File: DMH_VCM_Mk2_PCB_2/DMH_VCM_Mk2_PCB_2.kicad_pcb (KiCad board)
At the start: 2 copper layers, 48 x 175 mm, 95 parts, among them J1 TS_Jack_6.35mm_Sw, J10 TS_Jack_6.35mm_Sw, J100 IDC_02x05, J2 TS_Jack_6.35mm_Sw, J200 IDC_02x05, J3 TS_Jack_6.35mm_Sw, J4 TS_Jack_6.35mm_Sw, J5 TS_Jack_6.35mm_Sw, J50 Conn_01x08, J6 TS_Jack_6.35mm_Sw, J60 Conn_01x08, J7 TS_Jack_6.35mm_Sw, J70 Conn_01x08, J8 TS_Jack_6.35mm_Sw, J9 TS_Jack_6.35mm_Sw, Q1 BC548, Q2 BC548, Q3 BC548, Q4 BC548, Q5 BC548, Q6 BC548, U1 TL074, U2 TL074, U3 TL074

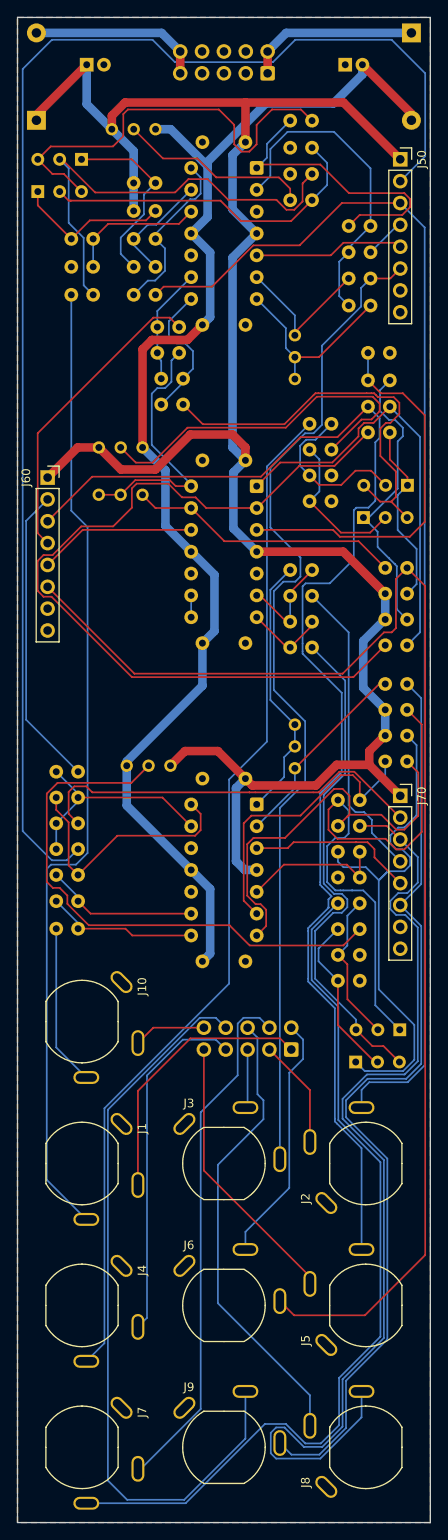
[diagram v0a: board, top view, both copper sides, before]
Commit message: Positioned PCB 2 components
Volume conflict with headers, needs correction o PCB 1
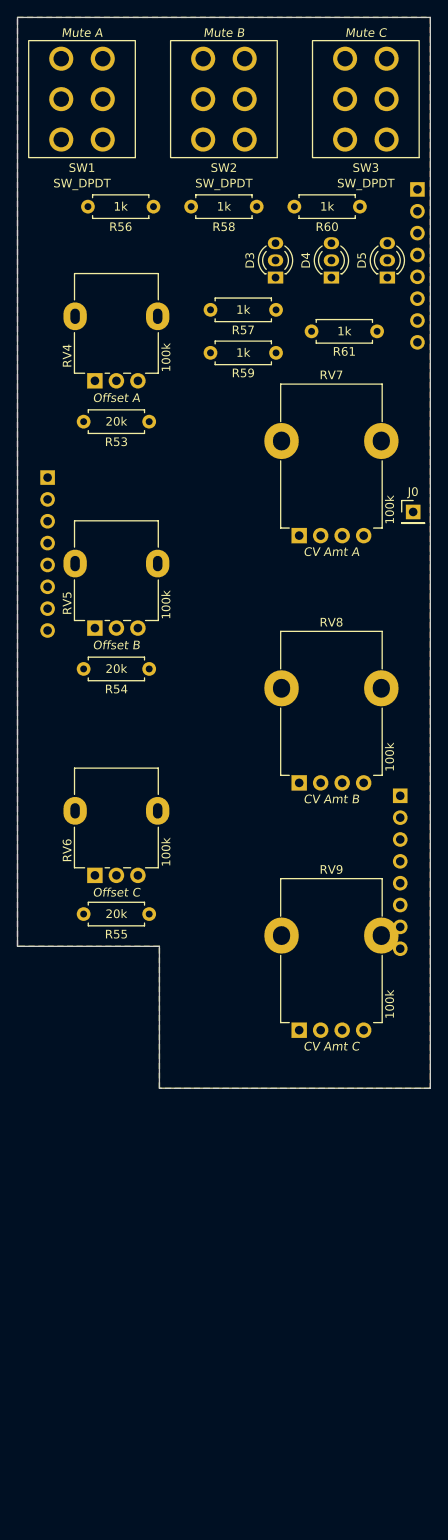
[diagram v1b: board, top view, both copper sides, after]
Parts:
- removed C1, C2: 47uF, Capacitor_THT:CP_Radial_D5.0mm_P2.00mm
- removed C3, C4, C5, C6, C7, C8: 100nF, Capacitor_THT:C_Disc_D4.3mm_W1.9mm_P5.00mm
- removed D1: SB140+, Diode_THT:D_DO-41_SOD81_P10.16mm_Horizontal
- removed D2: SB140-, Diode_THT:D_DO-41_SOD81_P10.16mm_Horizontal
- removed J1, J10, J2, J3, J4, J5, J6, J7, J8, J9: TS_Jack_6.35mm_Sw, SynthStuff:CUI_MJ-63052A
- removed J100: IDC_02x05, SynthStuff:IDC-Header_2x05_P2.54mm_Vertical_Eurorack
- removed J200: IDC_02x05, SynthStuff:IDC-Header_2x05_P2.54mm_Vertical_BackBone
- removed Q1, Q2, Q3, Q4, Q5, Q6: BC548, Package_TO_SOT_THT:TO-92L_Inline_Wide
- removed R1, R16, R17, R2, R31, R32: 20k, Resistor_THT:R_Axial_DIN0207_L6.3mm_D2.5mm_P2.54mm_Vertical
- removed R10, R11, R25, R26, R40, R41: 100R, Resistor_THT:R_Axial_DIN0207_L6.3mm_D2.5mm_P2.54mm_Vertical
- removed R12, R19, R21, R27, R34, R36, R4, R42, R6: 10k, Resistor_THT:R_Axial_DIN0207_L6.3mm_D2.5mm_P2.54mm_Vertical
- removed R13, R28, R62: 33k, Resistor_THT:R_Axial_DIN0207_L6.3mm_D2.5mm_P2.54mm_Vertical
- removed R14, R15, R18, R22, R23, R24, R29, R3, R30, R33, R37, R38, R39, R44, R45, R46, R47, R48, R49, R50, R51, R63, R64, R65, R7, R8, R9: 100k, Resistor_THT:R_Axial_DIN0207_L6.3mm_D2.5mm_P2.54mm_Vertical
- removed R20, R35, R5, R52: 1k, Resistor_THT:R_Axial_DIN0207_L6.3mm_D2.5mm_P2.54mm_Vertical
- removed RV1, RV2, RV3: 100k, Potentiometer_THT:Potentiometer_Bourns_3296W_Vertical
- removed RV10, RV11, RV12: 50k, Potentiometer_THT:Potentiometer_Bourns_3296W_Vertical
- removed U1, U2, U3: TL074, Package_DIP:DIP-14_W7.62mm_Socket
- added D3: LED_Dual_AKA, SynthStuff:LED_D3.0mm-2color, F.Cu at (81.0, 70.8)
- added D4: LED_Dual_AKA, SynthStuff:LED_D3.0mm-2color, F.Cu at (87.5, 70.8)
- added D5: LED_Dual_AKA, SynthStuff:LED_D3.0mm-2color, F.Cu at (94.0, 70.8)
- added J0: Conn_01x01, Connector_PinHeader_2.54mm:PinHeader_1x01_P2.54mm_Vertical, F.Cu at (97.0, 100.0)
- added R53: 20k, Resistor_THT:R_Axial_DIN0207_L6.3mm_D2.5mm_P7.62mm_Horizontal, F.Cu at (66.3, 89.5)
- added R54: 20k, Resistor_THT:R_Axial_DIN0207_L6.3mm_D2.5mm_P7.62mm_Horizontal, F.Cu at (66.3, 118.2)
- added R55: 20k, Resistor_THT:R_Axial_DIN0207_L6.3mm_D2.5mm_P7.62mm_Horizontal, F.Cu at (66.3, 146.8)
- added R56: 1k, Resistor_THT:R_Axial_DIN0207_L6.3mm_D2.5mm_P7.62mm_Horizontal, F.Cu at (66.8, 64.5)
- added R57: 1k, Resistor_THT:R_Axial_DIN0207_L6.3mm_D2.5mm_P7.62mm_Horizontal, F.Cu at (81.1, 76.5)
- added R58: 1k, Resistor_THT:R_Axial_DIN0207_L6.3mm_D2.5mm_P7.62mm_Horizontal, F.Cu at (78.8, 64.5)
- added R59: 1k, Resistor_THT:R_Axial_DIN0207_L6.3mm_D2.5mm_P7.62mm_Horizontal, F.Cu at (81.1, 81.5)
- added R60: 1k, Resistor_THT:R_Axial_DIN0207_L6.3mm_D2.5mm_P7.62mm_Horizontal, F.Cu at (90.8, 64.5)
- added R61: 1k, Resistor_THT:R_Axial_DIN0207_L6.3mm_D2.5mm_P7.62mm_Horizontal, F.Cu at (92.8, 79.0)
- added RV4: 100k, SynthStuff:Potentiometer_Alpha_RD901F-40-00D_Single_Vertical, F.Cu at (60.0, 84.8)
- added RV5: 100k, SynthStuff:Potentiometer_Alpha_RD901F-40-00D_Single_Vertical, F.Cu at (60.0, 113.5)
- added RV6: 100k, SynthStuff:Potentiometer_Alpha_RD901F-40-00D_Single_Vertical, F.Cu at (60.0, 142.2)
- added RV7: 100k, SynthStuff:Potentiometer_TT_P110KH1, F.Cu at (85.0, 102.8)
- added RV8: 100k, SynthStuff:Potentiometer_TT_P110KH1, F.Cu at (85.0, 131.5)
- added RV9: 100k, SynthStuff:Potentiometer_TT_P110KH1, F.Cu at (85.0, 160.2)
- added SW1: SW_DPDT, SynthStuff:Toggle_Switch_2_Poles_TE, F.Cu at (58.5, 52.0)
- added SW2: SW_DPDT, SynthStuff:Toggle_Switch_2_Poles_TE, F.Cu at (75.0, 52.0)
- added SW3: SW_DPDT, SynthStuff:Toggle_Switch_2_Poles_TE, F.Cu at (91.5, 52.0)
- J50, J60, J70: footprint Connector_PinSocket_2.54mm:PinSocket_1x08_P2.54mm_Vertical -> Connector_PinHeader_2.54mm:PinHeader_1x08_P2.54mm_Vertical; moved to B.Cu
- moved J50 4.03 mm to (97.5, 62.5), turned to 180 degrees
- turned J60 to 180 degrees
- turned J70 to 180 degrees
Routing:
- net +12V: track 237.7 -> 0.00 mm
- net /Inputs and Outputs/Mute A Switch: track 162.7 -> 0.00 mm
- net /Inputs and Outputs/CV B Jack: track 155.7 -> 0.00 mm
- net /Inputs and Outputs/Output B Jack: track 154.7 -> 0.00 mm
- net -12V: track 152.4 -> 0.00 mm
- net /Inputs and Outputs/Output A Jack: track 144.9 -> 0.00 mm
- net /Inputs and Outputs/Input B Jack: track 119.8 -> 0.00 mm
- net /Inputs and Outputs/CV A Jack: track 118.0 -> 0.00 mm
- net /Inputs and Outputs/Output C Jack: track 117.2 -> 0.00 mm
- net /Inputs and Outputs/Input A Jack: track 113.9 -> 0.00 mm
- net /Inputs and Outputs/CV C Jack: track 109.0 -> 0.00 mm
- net /Inputs and Outputs/Input C Jack: track 102.3 -> 0.00 mm
- net Net-(U2A--): track 97.8 -> 0.00 mm
- net Net-(J200-Pin_9): track 87.1 -> 0.00 mm
- net Net-(Q5-C): track 65.7 -> 0.00 mm
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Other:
- board size 48 x 175 mm -> 48 x 124.5 mm

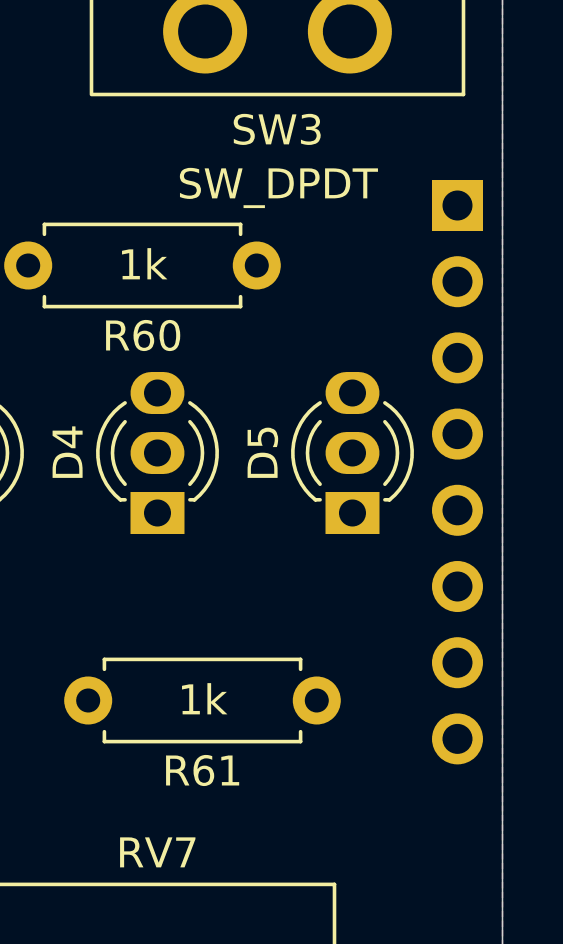
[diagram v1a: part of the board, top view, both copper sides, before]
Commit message: Resolved J50 volume conflict
J70 still to be solved
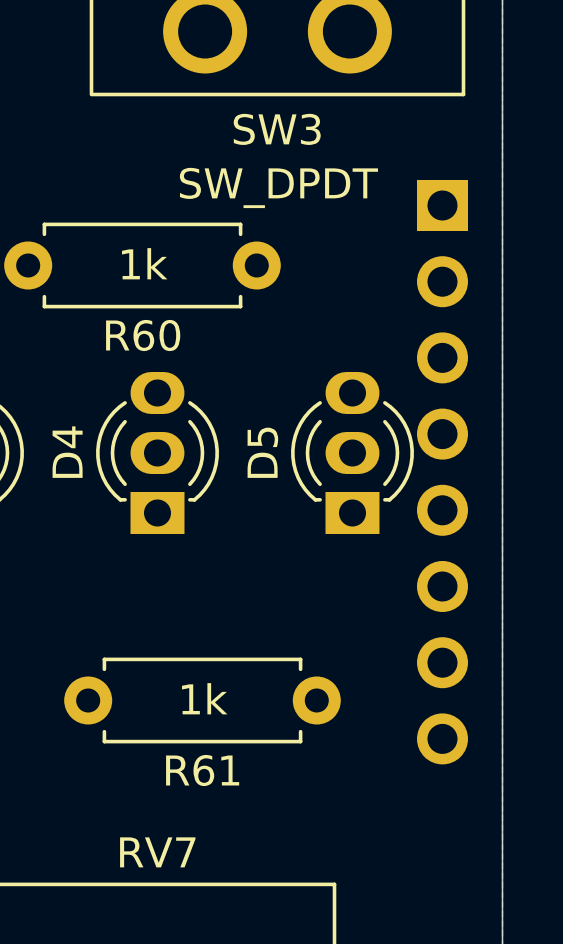
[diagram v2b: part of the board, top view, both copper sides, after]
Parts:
- moved J50 0.50 mm to (97.0, 62.5)
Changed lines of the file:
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@@
 	(net 35 "/Inputs and Outputs/CV Amt C Pot")
 	(footprint "SynthStuff:Toggle_Switch_2_Poles_TE"
+		(locked yes)
 		(layer "F.Cu")
 		(at 58.5 52 180)
@@
 	)
 	(footprint "SynthStuff:Potentiometer_TT_P110KH1"
+		(locked yes)
 		(layer "F.Cu")
 		(at 85 160.25)
@@
 	)
 	(footprint "SynthStuff:Potentiometer_Alpha_RD901F-40-00D_Single_Vertical"
+		(locked yes)
 		(layer "F.Cu")
 		(at 60 113.5 90)
@@
 	)
 	(footprint "SynthStuff:Potentiometer_TT_P110KH1"
+		(locked yes)
 		(layer "F.Cu")
 		(at 85 131.5)
@@
 	)
 	(footprint "SynthStuff:Potentiometer_TT_P110KH1"
+		(locked yes)
 		(layer "F.Cu")
 		(at 85 102.75)
@@
 	)
 	(footprint "SynthStuff:LED_D3.0mm-2color"
+		(locked yes)
 		(layer "F.Cu")
 		(at 81 70.75 90)
@@
 	)
 	(footprint "SynthStuff:LED_D3.0mm-2color"
+		(locked yes)
 		(layer "F.Cu")
 		(at 94 70.75 90)
@@
 	)
 	(footprint "SynthStuff:Potentiometer_Alpha_RD901F-40-00D_Single_Vertical"
+		(locked yes)
 		(layer "F.Cu")
 		(at 60 84.75 90)
@@
 	)
 	(footprint "SynthStuff:Potentiometer_Alpha_RD901F-40-00D_Single_Vertical"
+		(locked yes)
 		(layer "F.Cu")
 		(at 60 142.25 90)
@@
 	)
 	(footprint "SynthStuff:Toggle_Switch_2_Poles_TE"
+		(locked yes)
 		(layer "F.Cu")
 		(at 75 52 180)
@@
 	)
 	(footprint "SynthStuff:Toggle_Switch_2_Poles_TE"
+		(locked yes)
 		(layer "F.Cu")
 		(at 91.5 52 180)
@@
 	)
 	(footprint "SynthStuff:LED_D3.0mm-2color"
+		(locked yes)
 		(layer "F.Cu")
 		(at 87.5 70.75 90)
@@
 	)
 	(footprint "Connector_PinHeader_2.54mm:PinHeader_1x08_P2.54mm_Vertical"
+		(locked yes)
 		(layer "B.Cu")
 		(at 95.5 133 180)
@@
 	)
 	(footprint "Connector_PinHeader_2.54mm:PinHeader_1x08_P2.54mm_Vertical"
+		(locked yes)
 		(layer "B.Cu")
-		(at 97.5 62.5 180)
+		(at 97 62.5 180)
 		(descr "Through hole straight pin header, 1x08, 2.54mm pitch, single row")
 		(tags "Through hole pin header THT 1x08 2.54mm single row")

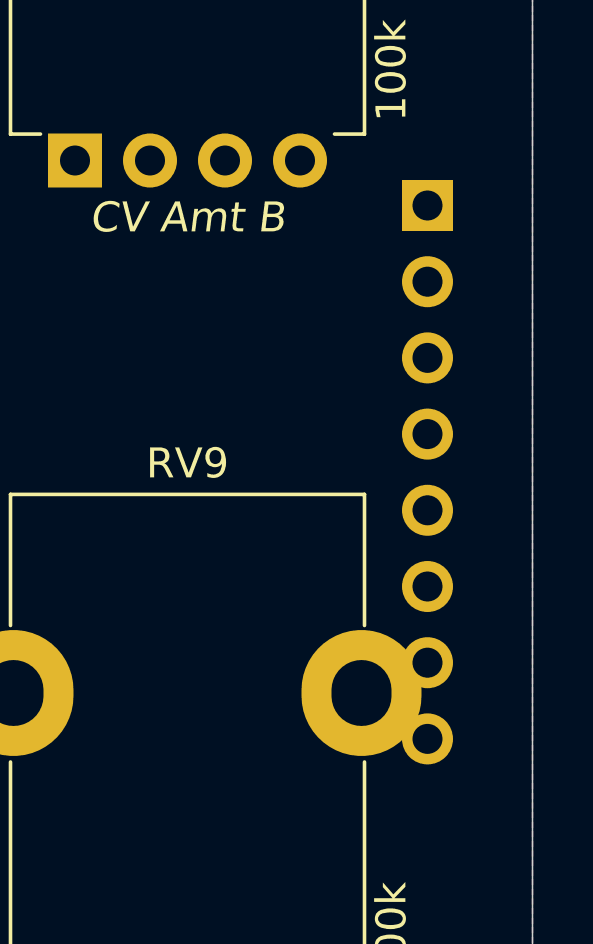
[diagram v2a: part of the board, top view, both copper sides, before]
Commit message: Resolved J70 volume conflict
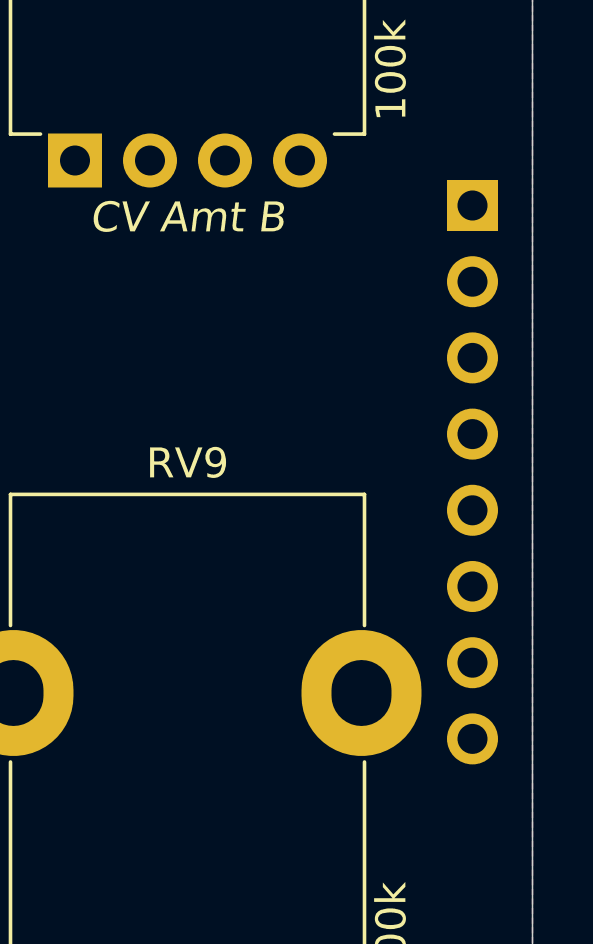
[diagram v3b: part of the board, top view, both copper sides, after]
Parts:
- moved J70 1.50 mm to (97.0, 133.0)
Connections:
- J70 pad 7: GND -> unconnected-(J70-Pin_7-Pad7)
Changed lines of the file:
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@@
 	(net 34 "/Inputs and Outputs/CV Amt B Pot")
 	(net 35 "/Inputs and Outputs/CV Amt C Pot")
+	(net 36 "unconnected-(J70-Pin_7-Pad7)")
 	(footprint "SynthStuff:Toggle_Switch_2_Poles_TE"
 		(locked yes)
@@
 		(locked yes)
 		(layer "B.Cu")
-		(at 95.5 133 180)
+		(at 97 133 180)
 		(descr "Through hole straight pin header, 1x08, 2.54mm pitch, single row")
 		(tags "Through hole pin header THT 1x08 2.54mm single row")
@@
 			(layers "*.Cu" "*.Mask")
 			(remove_unused_layers no)
-			(net 2 "GND")
+			(net 36 "unconnected-(J70-Pin_7-Pad7)")
 			(pinfunction "Pin_7")
-			(pintype "passive")
+			(pintype "passive+no_connect")
 		)
 		(pad "8" thru_hole oval
@@
 	)
 	(footprint "Connector_PinHeader_2.54mm:PinHeader_1x08_P2.54mm_Vertical"
+		(locked yes)
 		(layer "B.Cu")
 		(at 54.5 96 180)

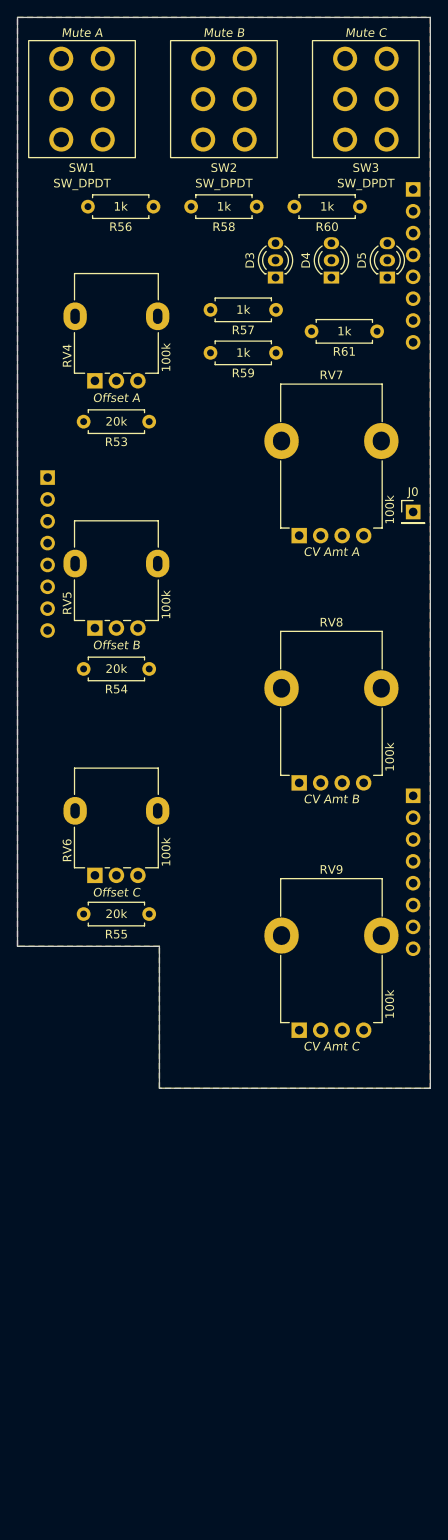
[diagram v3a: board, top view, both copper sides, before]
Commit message: Finished routing PCB 2
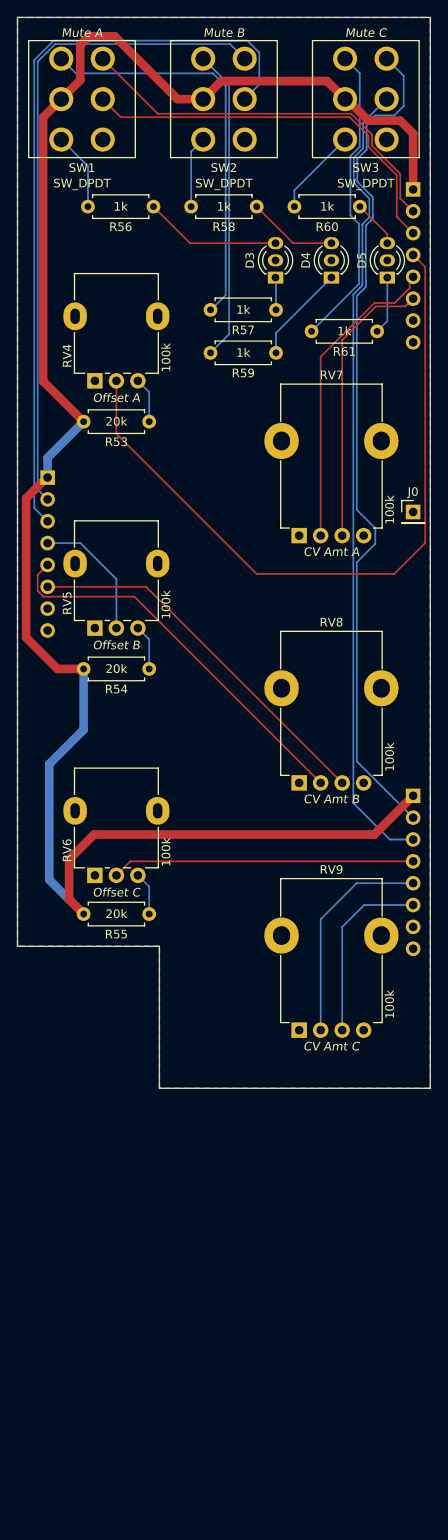
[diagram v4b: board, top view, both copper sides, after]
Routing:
- net +12V: track 0.00 -> 217.6 mm
- net /Inputs and Outputs/Mute C Switch: track 0.00 -> 98.6 mm
- net /Inputs and Outputs/Output C Jack: track 0.00 -> 93.6 mm
- net /Inputs and Outputs/Output B Jack: track 0.00 -> 88.0 mm
- net /Inputs and Outputs/Offset A Pot: track 0.00 -> 84.4 mm
- net /Inputs and Outputs/Mute B Switch: track 0.00 -> 77.0 mm
- net Net-(R57-Pad2): track 0.00 -> 47.2 mm
- net /Inputs and Outputs/Output A Jack: track 0.00 -> 46.1 mm
- net /Inputs and Outputs/Mute A Switch: track 0.00 -> 45.9 mm
- net /Inputs and Outputs/CV Amt B Pot: track 0.00 -> 45.6 mm
- net /Inputs and Outputs/CV B Jack: track 0.00 -> 43.7 mm
- net Net-(R59-Pad2): track 0.00 -> 36.3 mm
- net /Inputs and Outputs/CV Amt A Pot: track 0.00 -> 35.9 mm
- net Net-(R61-Pad2): track 0.00 -> 35.5 mm
- net /Inputs and Outputs/Offset C Pot: track 0.00 -> 35.2 mm
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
